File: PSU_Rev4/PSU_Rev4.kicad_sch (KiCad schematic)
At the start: 96 parts, among them J101 BATTERY, J102 I2C, J103 USB_C, J104 PWR, J105 DATA1, Q101 BSH205G2A, Q102 DMP6050SSD, Q103 2N7002H, SW101 SW_SPDT, U101 TPS63070, U102 MCP73834T, U103 NCV33163, U104 CYPD3177-24LQ, U105 CS5173

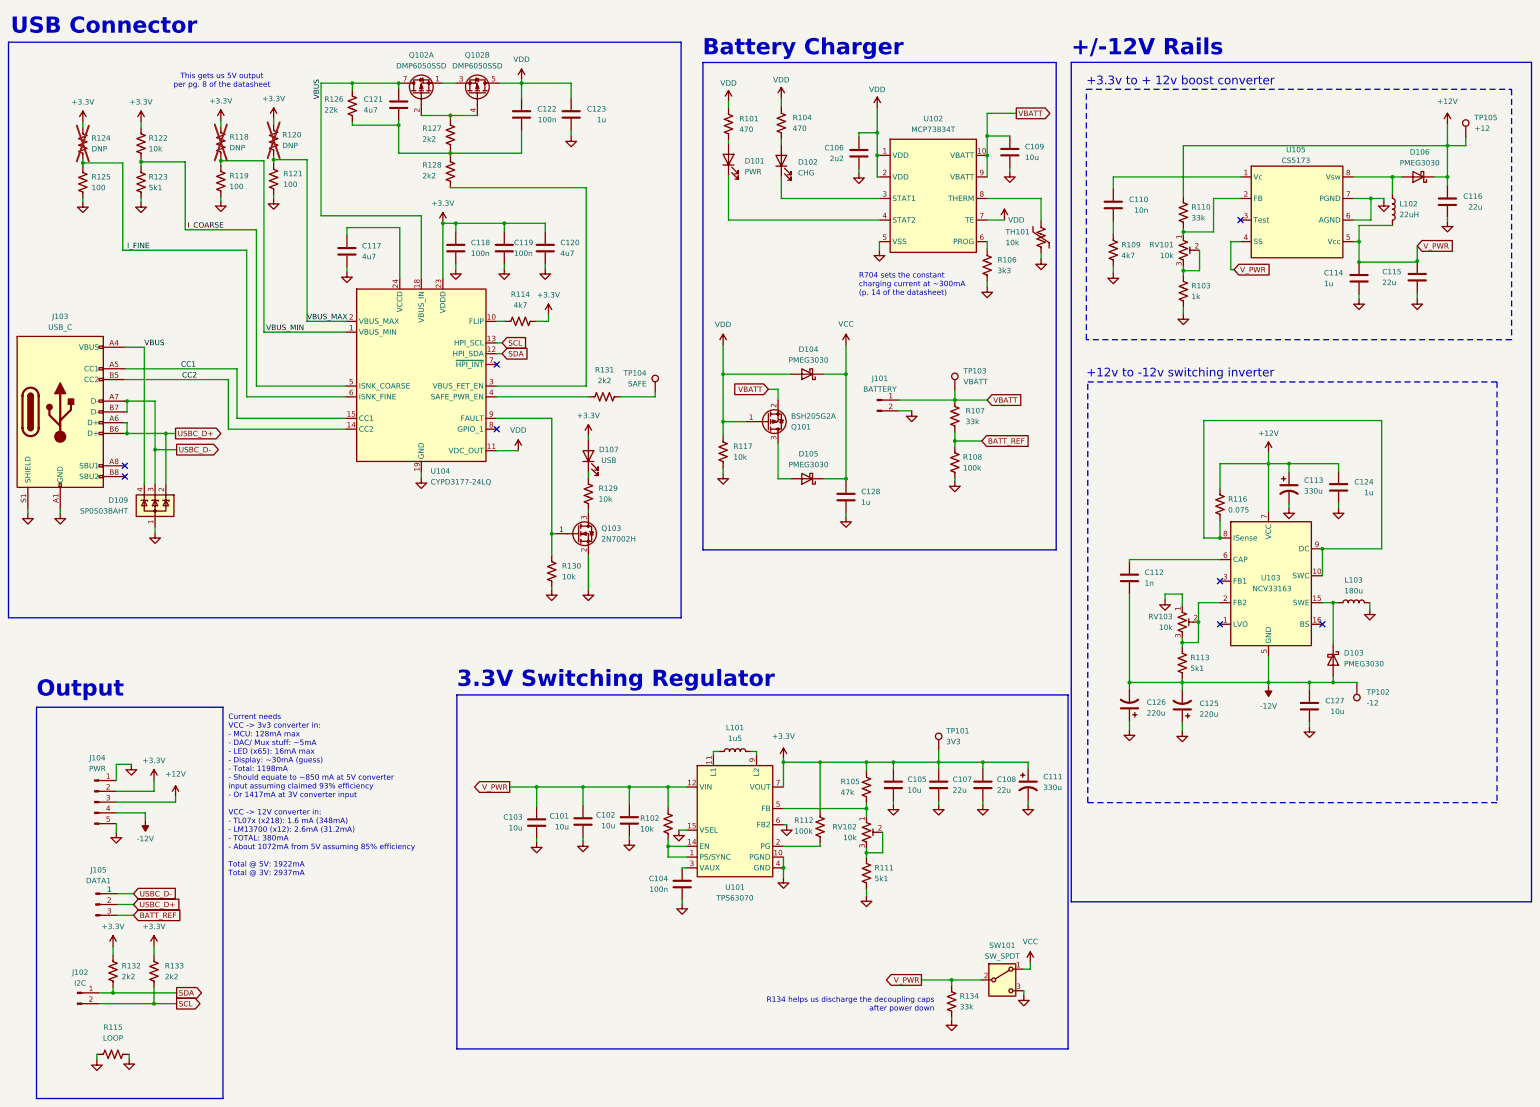
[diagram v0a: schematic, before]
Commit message: psu schematic updates
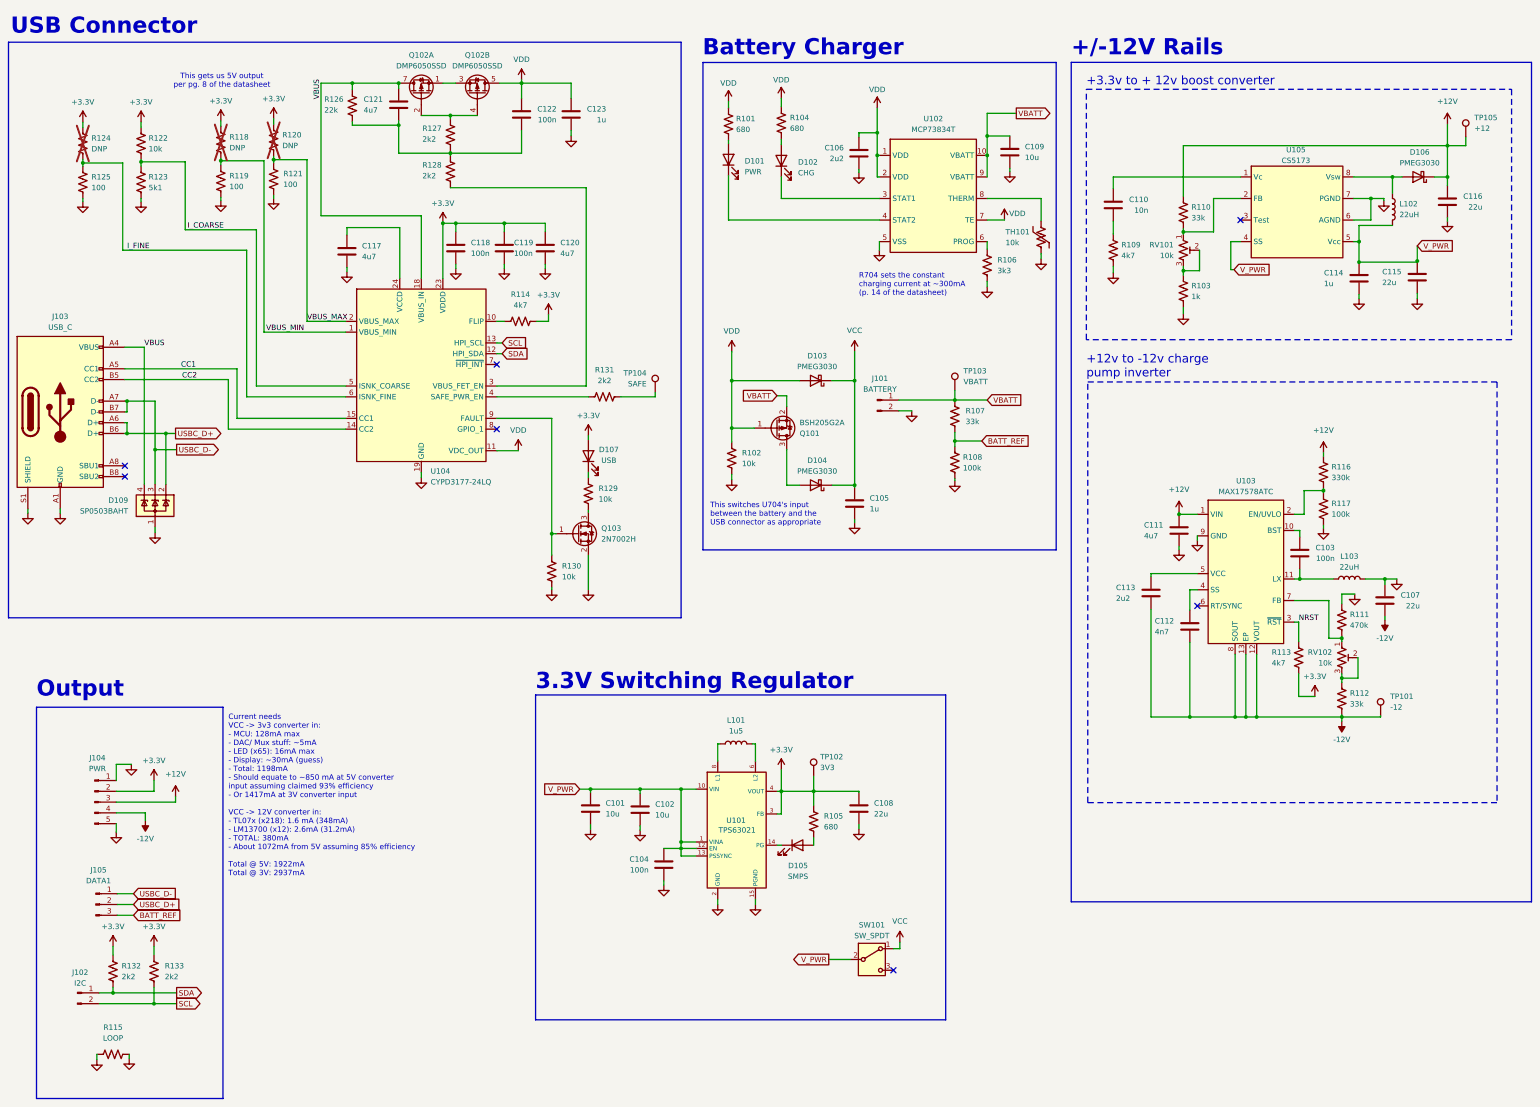
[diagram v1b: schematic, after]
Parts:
- removed C111, C113: 330u, Capacitor_THT:CP_Radial_D5.0mm_P2.50mm, symbol Device:C_Polarized_US
- removed C124, C128: 1u, Capacitor_SMD:C_0805_2012Metric, symbol Device:C
- removed C125, C126: 220u, Capacitor_THT:CP_Radial_D5.0mm_P2.50mm, symbol Device:C_Polarized_US
- removed C127: 10u, Capacitor_SMD:C_0805_2012Metric, symbol Device:C
- removed D105: PMEG3030, Diode_SMD:D_SOD-123, symbol Device:D_Schottky
- removed R134: 33k, Resistor_SMD:R_0805_2012Metric, symbol Device:R_US
- removed RV103: 10k, Potentiometer_THT:Potentiometer_Bourns_3296W_Vertical, symbol Device:R_Potentiometer_Trim_US
- removed U101: TPS63070, Package_DFN_QFN:TXN_QFN15, symbol Regulator_Switching:TPS63070
- removed U103: NCV33163, Package_SO:SOIC-16W_7.5x10.3mm_P1.27mm, symbol Regulator_Switching:NCV33163
- added C111: 4u7, Capacitor_SMD:C_0805_2012Metric, symbol Device:C
- added C113: 2u2, Capacitor_SMD:C_0805_2012Metric, symbol Device:C
- added D105: SMPS, LED_THT:LED_D3.0mm, symbol Device:LED
- added U101: TPS63021, Package_SON:Texas_S-PVSON-N14, symbol Regulator_Switching:TPS63021
- added U103: MAX17578ATC, Package_DFN_QFN:TDFN-12-1EP_3x3mm_P0.4mm_EP1.7x2.45mm, symbol Regulator_Switching:MAX17578ATC
- C103: value 10u -> 100n
- C105: value 10u -> 1u
- C112: value 1n -> 4n7
- L103: value 180u -> 22uH; footprint Inductor_SMD:L_Coilcraft_MSS1278-XXX -> Inductor_SMD:L_Changjiang_FNR4010S
- R101, R104: value 470 -> 680
- R105: value 47k -> 680
- R111: value 5k1 -> 470k
- R112: value 100k -> 33k
- R113: value 5k1 -> 4k7
- R116: value 0.075 -> 330k
- R117: value 10k -> 100k
- TP101: value 3V3 -> -12
- TP102: value -12 -> 3V3
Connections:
- net +12V: now also C111.1, U103.1 (VIN)
- net +3.3V: now also R113.2, TP102.1, U101.3 (FB), U101.4 (VOUT), U101.5 (VOUT); no longer C105.1, C107.1, R112.1, TP101.1
- net -12V: now also C107.2, R112.2, TP101.1, C113.2, U103.12 (VOUT), U103.13 (EP), U103.8 (SOUT); no longer D103.2 (A), R113.2, TP102.1
- net GND: now also C107.1, R102.2, R111.1, C111.2, U101.15 (PGND), U101.2 (GND), U103.9 (GND); no longer C103.2, C107.2, R111.2, SW101.3 (C)
- net VCC: now also C105.1, D103.1 (K)
- net VDD: now also D103.2 (A), R102.1; no longer D104.2 (A), R117.1
- net VIN: now also C104.1, U101.1 (VINA), U101.10 (VIN), U101.11 (VIN), U101.12 (EN), U101.13 (PSSYNC); no longer C103.1, R102.1
- net at RV102.1: now also R111.2, U103.7 (FB); no longer R105.2
- net at R116.2: now also R117.1, U103.2 (EN/UVLO)
- net NRST: now reaches R113.1
- net NRST: now also U103.3 (~{RST})
- net at L101.1: now also U101.8 (L1), U101.9 (L1)
- net at L101.2: now also U101.6 (L2), U101.7 (L2)
- net at Q101.3 (D): now also D104.2 (A)
- net at RV102.2, RV102.3: now also R112.1; no longer R111.1
- net at C112.1: now also U103.4 (SS)
- net at L103.1: now also C103.2, U103.11 (LX); no longer D103.1 (K)
- new net: D105.1 (K), U101.14 (PG)
- new net: C103.1, U103.10 (BST)
- new net: C113.1, U103.5 (VCC)
- new net: D105.2 (A), R105.2
- no-connect marks 8 -> 7
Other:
- note added: "+12v to -12v charge pump inverter"
- note added: "This switches U704's input between the battery and the USB connector as appropriate"
- note removed: "+12v to -12v switching inverter"
- note removed: "R134 helps us discharge the decoupling caps after power down"
- moved on the sheet: L101, SW101
